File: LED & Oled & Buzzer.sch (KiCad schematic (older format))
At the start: 16 parts, among them J6 Conn_01x04, Q4 BC847

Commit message: Major upgrade
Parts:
- BZ1: value SMT-0825-T-2 -> CMT-5023S; footprint Buzzer_Beeper:PUIAudio_SMT_0825_S_4_R -> CMT-5023S-SMT-TR:CMT5023SSMTTR
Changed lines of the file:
@@
 P 3700 3800
 F 0 "BZ1" H 3852 3829 50  0000 L CNN
-F 1 "SMT-0825-T-2" H 3852 3738 50  0000 L CNN
-F 2 "Buzzer_Beeper:PUIAudio_SMT_0825_S_4_R" V 3675 3900 50  0001 C CNN
+F 1 "CMT-5023S" H 3852 3738 50  0000 L CNN
+F 2 "CMT-5023S-SMT-TR:CMT5023SSMTTR" V 3675 3900 50  0001 C CNN
 F 3 "~" V 3675 3900 50  0001 C CNN
 	1    3700 3800

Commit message: New footprint for OLED connector
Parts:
- J6: footprint (none) -> Connector_PinHeader_1.27mm:PinHeader_1x04_P1.27mm_Vertical_SMD_Pin1Left
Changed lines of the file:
@@
 F 0 "J6" H 3780 2342 50  0000 L CNN
 F 1 "Conn_01x04" H 3780 2251 50  0000 L CNN
-F 2 "" H 3700 2350 50  0001 C CNN
+F 2 "Connector_PinHeader_1.27mm:PinHeader_1x04_P1.27mm_Vertical_SMD_Pin1Left" H 3700 2350 50  0001 C CNN
 F 3 "~" H 3700 2350 50  0001 C CNN
 	1    3700 2350

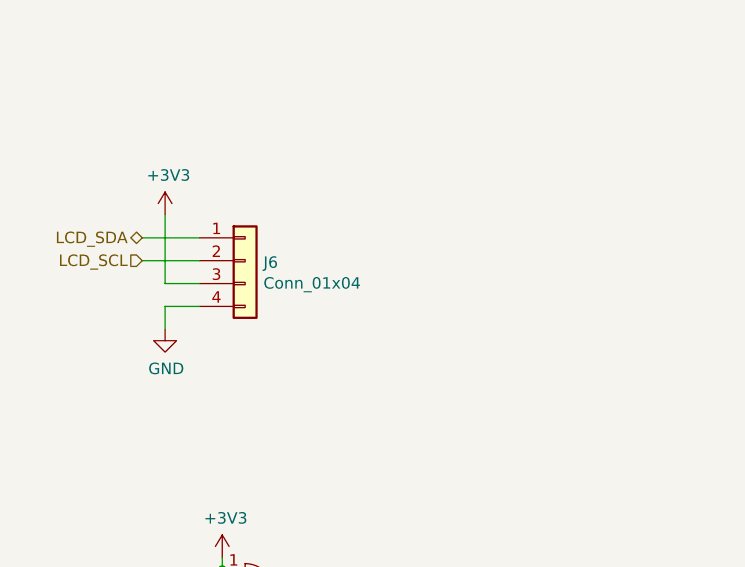
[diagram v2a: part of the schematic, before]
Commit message: Changed connector for OLED
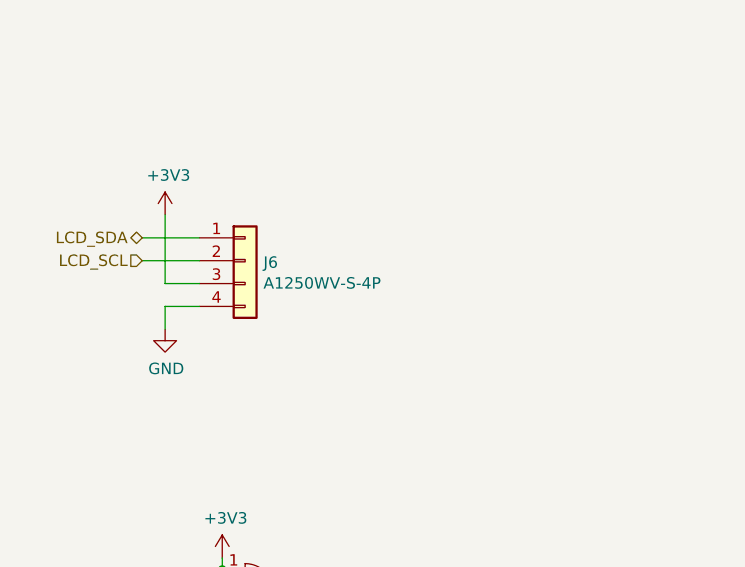
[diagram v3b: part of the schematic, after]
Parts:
- J6: value Conn_01x04 -> A1250WV-S-4P; footprint Connector_PinHeader_1.27mm:PinHeader_1x04_P1.27mm_Vertical_SMD_Pin1Left -> Connector_JST:JST_GH_BM04B-GHS-TBT_1x04-1MP_P1.25mm_Vertical
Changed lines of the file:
@@
 P 3700 2350
 F 0 "J6" H 3780 2342 50  0000 L CNN
-F 1 "Conn_01x04" H 3780 2251 50  0000 L CNN
-F 2 "Connector_PinHeader_1.27mm:PinHeader_1x04_P1.27mm_Vertical_SMD_Pin1Left" H 3700 2350 50  0001 C CNN
+F 1 "A1250WV-S-4P" H 3780 2251 50  0000 L CNN
+F 2 "Connector_JST:JST_GH_BM04B-GHS-TBT_1x04-1MP_P1.25mm_Vertical" H 3700 2350 50  0001 C CNN
 F 3 "~" H 3700 2350 50  0001 C CNN
 	1    3700 2350

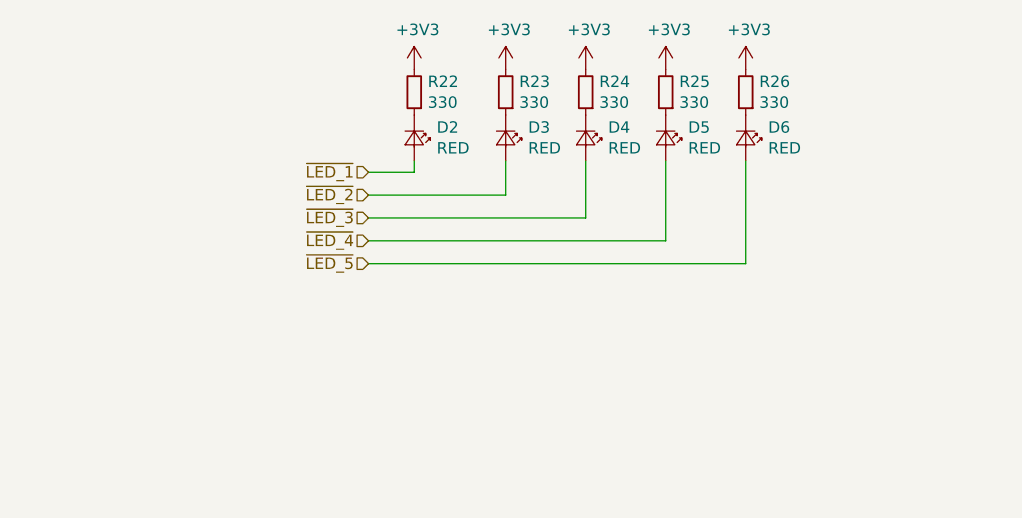
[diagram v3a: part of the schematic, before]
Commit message: Added led
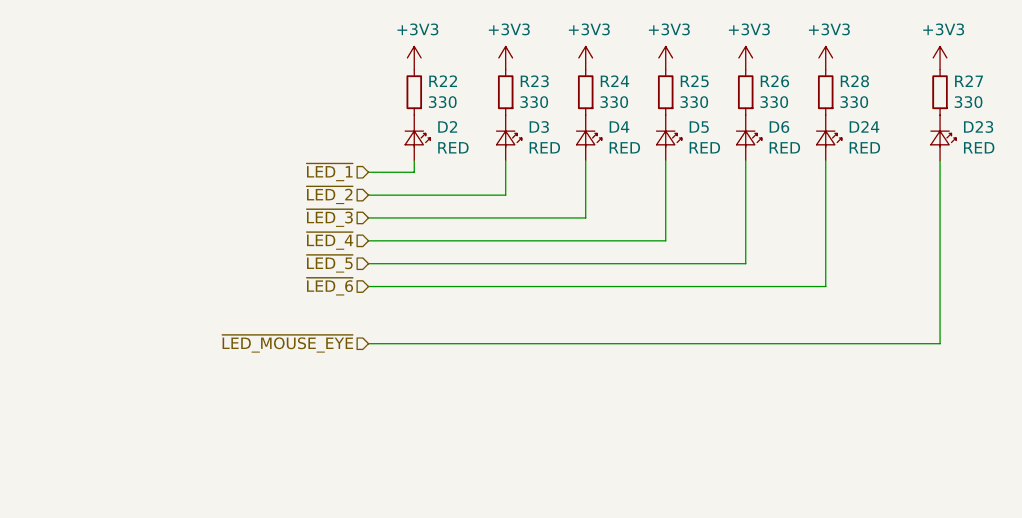
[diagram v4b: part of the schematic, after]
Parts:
- added D23, D24: RED, LED_SMD:LED_0402_1005Metric, symbol Device:LED_Small
- added R27, R28: 330, Resistor_SMD:R_0402_1005Metric, symbol Device:R_Small
- D6: footprint LED_SMD:LED_0603_1608Metric -> LED_SMD:LED_0402_1005Metric
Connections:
- net +3V3: now also R27.2, R28.2
- new net: D23.1 (K), R27.1
- new net: D24.1 (K), R28.1
- new net ~LED_6: D24.2 (A)
- new net ~LED_MOUSE_EYE: D23.2 (A)
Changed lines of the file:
@@
-$EndComp
-$Comp
-L Device:LED_Small D6
-U 1 1 5E6C8415
-P 8050 1700
-F 0 "D6" V 8004 1798 50  0000 L CNN
-F 1 "RED" V 8095 1798 50  0000 L CNN
-F 2 "LED_SMD:LED_0603_1608Metric" V 8050 1700 50  0001 C CNN
-F 3 "~" V 8050 1700 50  0001 C CNN
-	1    8050 1700
-	0    1    1    0
-$EndComp
-$Comp
-L power:+3V3 #PWR0200
-U 1 1 5E6C841B
-P 8050 1400
-F 0 "#PWR0200" H 8050 1250 50  0001 C CNN
-F 1 "+3V3" H 8065 1573 50  0000 C CNN
-F 2 "" H 8050 1400 50  0001 C CNN
-F 3 "" H 8050 1400 50  0001 C CNN
-	1    8050 1400
-	1    0    0    -1
 $EndComp
 $Comp
@@
 	3600 3900 3500 3900
 Connection ~ 3600 3900
+$Comp
+L power:+3V3 #PWR0200
+U 1 1 5E6C841B
+P 8050 1400
+F 0 "#PWR0200" H 8050 1250 50  0001 C CNN
+F 1 "+3V3" H 8065 1573 50  0000 C CNN
+F 2 "" H 8050 1400 50  0001 C CNN
+F 3 "" H 8050 1400 50  0001 C CNN
+	1    8050 1400
+	1    0    0    -1
+$EndComp
+$Comp
+L Device:LED_Small D6
+U 1 1 5E6C8415
+P 8050 1700
+F 0 "D6" V 8004 1798 50  0000 L CNN
+F 1 "RED" V 8095 1798 50  0000 L CNN
+F 2 "LED_SMD:LED_0402_1005Metric" V 8050 1700 50  0001 C CNN
+F 3 "~" V 8050 1700 50  0001 C CNN
+	1    8050 1700
+	0    1    1    0
+$EndComp
+$Comp
+L Device:R_Small R27
+U 1 1 5E7C2F0B
+P 8900 1500
+F 0 "R27" H 8841 1454 50  0000 R CNN
+F 1 "330" H 8841 1545 50  0000 R CNN
+F 2 "Resistor_SMD:R_0402_1005Metric" H 8900 1500 50  0001 C CNN
+F 3 "~" H 8900 1500 50  0001 C CNN
+	1    8900 1500
+	-1   0    0    1
+$EndComp
+$Comp
+L power:+3V3 #PWR0187
+U 1 1 5E7C2F12
+P 8900 1400
+F 0 "#PWR0187" H 8900 1250 50  0001 C CNN
+F 1 "+3V3" H 8915 1573 50  0000 C CNN
+F 2 "" H 8900 1400 50  0001 C CNN
+F 3 "" H 8900 1400 50  0001 C CNN
+	1    8900 1400
+	1    0    0    -1
+$EndComp
+$Comp
+L Device:LED_Small D23
+U 1 1 5E7C2F18
+P 8900 1700
+F 0 "D23" V 8854 1798 50  0000 L CNN
+F 1 "RED" V 8945 1798 50  0000 L CNN
+F 2 "LED_SMD:LED_0402_1005Metric" V 8900 1700 50  0001 C CNN
+F 3 "~" V 8900 1700 50  0001 C CNN
+	1    8900 1700
+	0    1    1    0
+$EndComp
+Wire Wire Line
+	8900 2600 6400 2600
+Text HLabel 6400 2600 0    50   Input ~ 0
+~LED_MOUSE_EYE
+$Comp
+L Device:R_Small R28
+U 1 1 5E9978CE
+P 8400 1500
+F 0 "R28" H 8341 1454 50  0000 R CNN
+F 1 "330" H 8341 1545 50  0000 R CNN
+F 2 "Resistor_SMD:R_0402_1005Metric" H 8400 1500 50  0001 C CNN
+F 3 "~" H 8400 1500 50  0001 C CNN
+	1    8400 1500
+	-1   0    0    1
+$EndComp
+$Comp
+L power:+3V3 #PWR0189
+U 1 1 5E9978D5
+P 8400 1400
+F 0 "#PWR0189" H 8400 1250 50  0001 C CNN
+F 1 "+3V3" H 8415 1573 50  0000 C CNN
+F 2 "" H 8400 1400 50  0001 C CNN
+F 3 "" H 8400 1400 50  0001 C CNN
+	1    8400 1400
+	1    0    0    -1
+$EndComp
+$Comp
+L Device:LED_Small D24
+U 1 1 5E9978DB
+P 8400 1700
+F 0 "D24" V 8354 1798 50  0000 L CNN
+F 1 "RED" V 8445 1798 50  0000 L CNN
+F 2 "LED_SMD:LED_0402_1005Metric" V 8400 1700 50  0001 C CNN
+F 3 "~" V 8400 1700 50  0001 C CNN
+	1    8400 1700
+	0    1    1    0
+$EndComp
+Wire Wire Line
+	8400 2350 6400 2350
+Wire Wire Line
+	8400 1800 8400 2350
+Wire Wire Line
+	8900 1800 8900 2600
+Text HLabel 6400 2350 0    50   Input ~ 0
+~LED_6
 $EndSCHEMATC

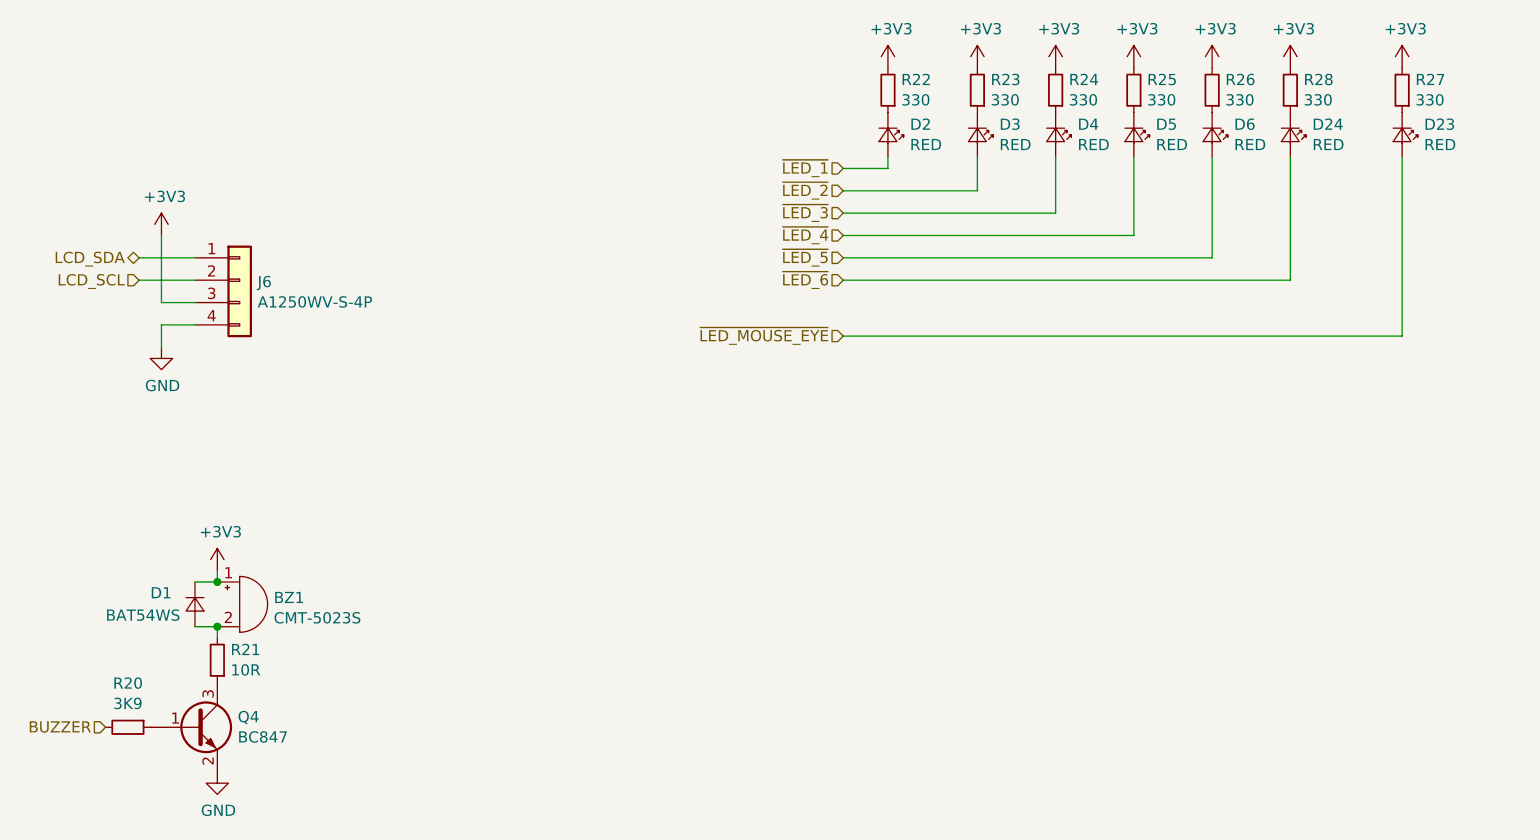
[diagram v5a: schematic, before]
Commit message: Changes in graphics, tweaks in power input, resistor values
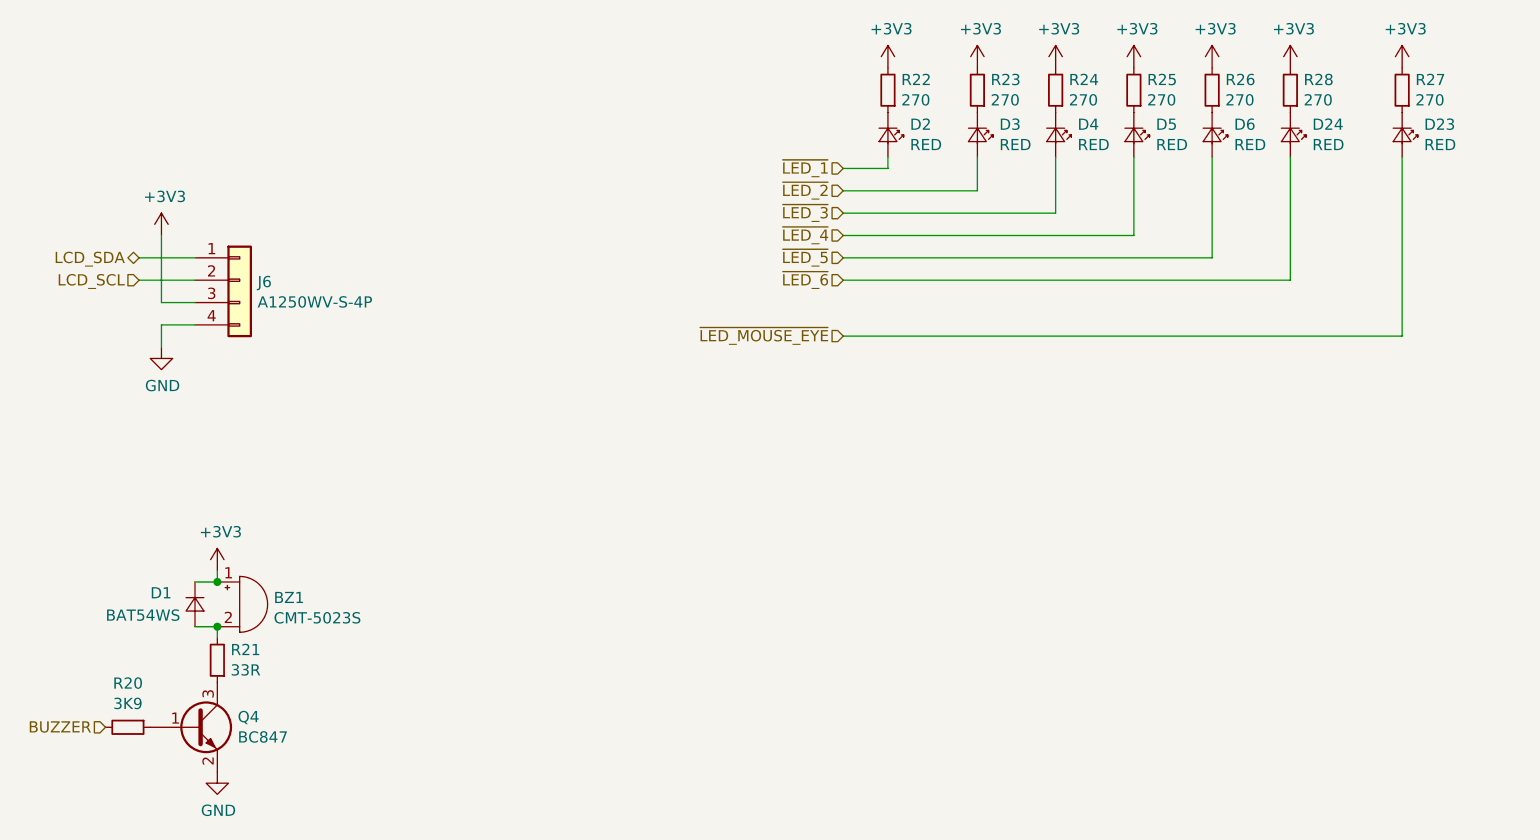
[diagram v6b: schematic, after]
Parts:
- R21: value 10R -> 33R
- R22, R23, R24, R25, R26, R27, R28: value 330 -> 270
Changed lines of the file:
@@
 P 3600 4050
 F 0 "R21" H 3541 4004 50  0000 R CNN
-F 1 "10R" H 3541 4095 50  0000 R CNN
+F 1 "33R" H 3541 4095 50  0000 R CNN
 F 2 "Resistor_SMD:R_0402_1005Metric" H 3600 4050 50  0001 C CNN
 F 3 "~" H 3600 4050 50  0001 C CNN
@@
 P 6600 1500
 F 0 "R22" H 6541 1454 50  0000 R CNN
-F 1 "330" H 6541 1545 50  0000 R CNN
+F 1 "270" H 6541 1545 50  0000 R CNN
 F 2 "Resistor_SMD:R_0402_1005Metric" H 6600 1500 50  0001 C CNN
 F 3 "~" H 6600 1500 50  0001 C CNN
@@
 P 7000 1500
 F 0 "R23" H 6941 1454 50  0000 R CNN
-F 1 "330" H 6941 1545 50  0000 R CNN
+F 1 "270" H 6941 1545 50  0000 R CNN
 F 2 "Resistor_SMD:R_0402_1005Metric" H 7000 1500 50  0001 C CNN
 F 3 "~" H 7000 1500 50  0001 C CNN
@@
 P 7350 1500
 F 0 "R24" H 7291 1454 50  0000 R CNN
-F 1 "330" H 7291 1545 50  0000 R CNN
+F 1 "270" H 7291 1545 50  0000 R CNN
 F 2 "Resistor_SMD:R_0402_1005Metric" H 7350 1500 50  0001 C CNN
 F 3 "~" H 7350 1500 50  0001 C CNN
@@
 P 7700 1500
 F 0 "R25" H 7641 1454 50  0000 R CNN
-F 1 "330" H 7641 1545 50  0000 R CNN
+F 1 "270" H 7641 1545 50  0000 R CNN
 F 2 "Resistor_SMD:R_0402_1005Metric" H 7700 1500 50  0001 C CNN
 F 3 "~" H 7700 1500 50  0001 C CNN
@@
 P 8050 1500
 F 0 "R26" H 7991 1454 50  0000 R CNN
-F 1 "330" H 7991 1545 50  0000 R CNN
+F 1 "270" H 7991 1545 50  0000 R CNN
 F 2 "Resistor_SMD:R_0402_1005Metric" H 8050 1500 50  0001 C CNN
 F 3 "~" H 8050 1500 50  0001 C CNN
@@
 P 8900 1500
 F 0 "R27" H 8841 1454 50  0000 R CNN
-F 1 "330" H 8841 1545 50  0000 R CNN
+F 1 "270" H 8841 1545 50  0000 R CNN
 F 2 "Resistor_SMD:R_0402_1005Metric" H 8900 1500 50  0001 C CNN
 F 3 "~" H 8900 1500 50  0001 C CNN
@@
 P 8400 1500
 F 0 "R28" H 8341 1454 50  0000 R CNN
-F 1 "330" H 8341 1545 50  0000 R CNN
+F 1 "270" H 8341 1545 50  0000 R CNN
 F 2 "Resistor_SMD:R_0402_1005Metric" H 8400 1500 50  0001 C CNN
 F 3 "~" H 8400 1500 50  0001 C CNN

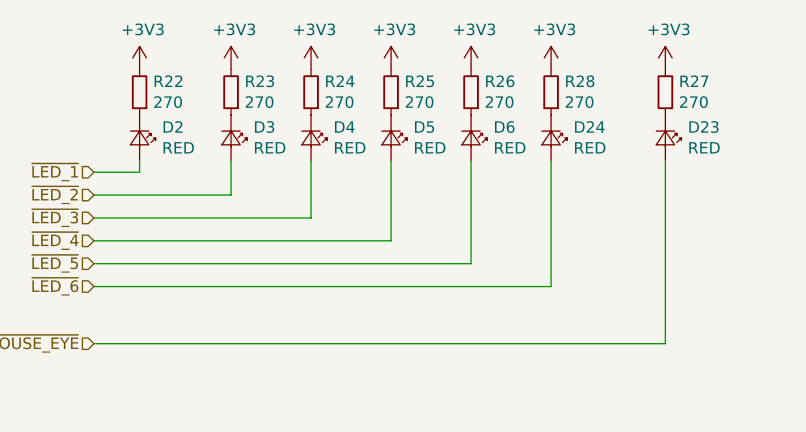
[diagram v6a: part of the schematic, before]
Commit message: Minor update in pin connections
Connected Mouse eye led to PWM output
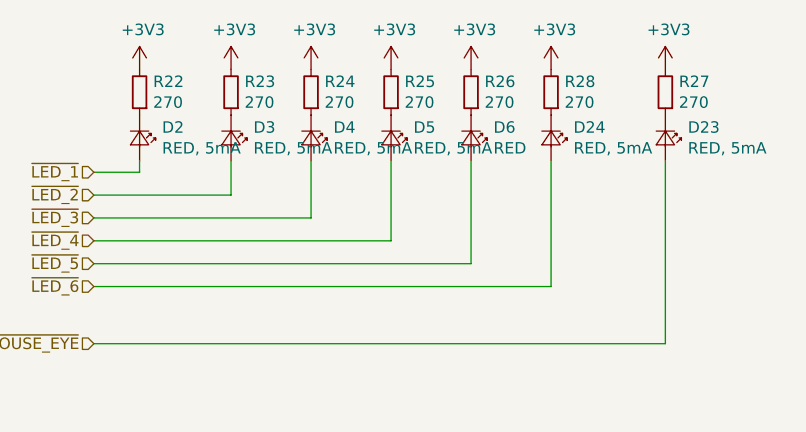
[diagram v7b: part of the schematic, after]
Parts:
- D2, D23, D24, D3, D4, D5: value RED -> RED, 5mA
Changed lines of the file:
@@
 P 6600 1700
 F 0 "D2" V 6554 1798 50  0000 L CNN
-F 1 "RED" V 6645 1798 50  0000 L CNN
+F 1 "RED, 5mA" V 6645 1798 50  0000 L CNN
 F 2 "LED_SMD:LED_0402_1005Metric" V 6600 1700 50  0001 C CNN
 F 3 "~" V 6600 1700 50  0001 C CNN
@@
 P 7000 1700
 F 0 "D3" V 6954 1798 50  0000 L CNN
-F 1 "RED" V 7045 1798 50  0000 L CNN
+F 1 "RED, 5mA" V 7045 1798 50  0000 L CNN
 F 2 "LED_SMD:LED_0402_1005Metric" V 7000 1700 50  0001 C CNN
 F 3 "~" V 7000 1700 50  0001 C CNN
@@
 P 7350 1700
 F 0 "D4" V 7304 1798 50  0000 L CNN
-F 1 "RED" V 7395 1798 50  0000 L CNN
+F 1 "RED, 5mA" V 7395 1798 50  0000 L CNN
 F 2 "LED_SMD:LED_0402_1005Metric" V 7350 1700 50  0001 C CNN
 F 3 "~" V 7350 1700 50  0001 C CNN
@@
 P 7700 1700
 F 0 "D5" V 7654 1798 50  0000 L CNN
-F 1 "RED" V 7745 1798 50  0000 L CNN
+F 1 "RED, 5mA" V 7745 1798 50  0000 L CNN
 F 2 "LED_SMD:LED_0402_1005Metric" V 7700 1700 50  0001 C CNN
 F 3 "~" V 7700 1700 50  0001 C CNN
@@
 P 8900 1700
 F 0 "D23" V 8854 1798 50  0000 L CNN
-F 1 "RED" V 8945 1798 50  0000 L CNN
+F 1 "RED, 5mA" V 8945 1798 50  0000 L CNN
 F 2 "LED_SMD:LED_0402_1005Metric" V 8900 1700 50  0001 C CNN
 F 3 "~" V 8900 1700 50  0001 C CNN
@@
 P 8400 1700
 F 0 "D24" V 8354 1798 50  0000 L CNN
-F 1 "RED" V 8445 1798 50  0000 L CNN
+F 1 "RED, 5mA" V 8445 1798 50  0000 L CNN
 F 2 "LED_SMD:LED_0402_1005Metric" V 8400 1700 50  0001 C CNN
 F 3 "~" V 8400 1700 50  0001 C CNN

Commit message: Issues
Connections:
- net ~LED_1: now also D2.1 (K); no longer D2.2 (A)
- net ~LED_2: now also D3.1 (K); no longer D3.2 (A)
- net ~LED_3: now also D4.1 (K); no longer D4.2 (A)
- net ~LED_4: now also D5.1 (K); no longer D5.2 (A)
- net ~LED_5: now also D6.1 (K); no longer D6.2 (A)
- net ~LED_6: now also D24.1 (K); no longer D24.2 (A)
- net at R22.1: now also D2.2 (A); no longer D2.1 (K)
- net at R23.1: now also D3.2 (A); no longer D3.1 (K)
- net at R24.1: now also D4.2 (A); no longer D4.1 (K)
- net at R25.1: now also D5.2 (A); no longer D5.1 (K)
- net at R26.1: now also D6.2 (A); no longer D6.1 (K)
- net at R28.1: now also D24.2 (A); no longer D24.1 (K)
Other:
- moved on the sheet: D2, D24, D3, D4, D5, D6
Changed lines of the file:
@@
 F 3 "~" V 6600 1700 50  0001 C CNN
 	1    6600 1700
-	0    1    1    0
+	0    -1   -1   0
 $EndComp
 $Comp
@@
 F 3 "~" V 7000 1700 50  0001 C CNN
 	1    7000 1700
-	0    1    1    0
+	0    -1   -1   0
 $EndComp
 $Comp
@@
 F 3 "~" V 7350 1700 50  0001 C CNN
 	1    7350 1700
-	0    1    1    0
+	0    -1   -1   0
 $EndComp
 $Comp
@@
 F 3 "~" V 7700 1700 50  0001 C CNN
 	1    7700 1700
-	0    1    1    0
+	0    -1   -1   0
 $EndComp
 $Comp
@@
 F 3 "~" V 8050 1700 50  0001 C CNN
 	1    8050 1700
-	0    1    1    0
+	0    -1   -1   0
 $EndComp
 $Comp
@@
 F 3 "~" V 8400 1700 50  0001 C CNN
 	1    8400 1700
-	0    1    1    0
-$EndComp
-Wire Wire Line
+	0    -1   -1   0
+$EndComp
+Wire Wire Line
